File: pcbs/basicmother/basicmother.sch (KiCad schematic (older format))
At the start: 18 parts, among them IC1 ATMEGA88-P, P1 DIL16, P2 CONN_02X05, P3 CONN_02X03, P4 CONN_01X02, P5 CONN_01X02, U1 ZIGBIT_DUAL_DIP, U2 MBED, X1 18.432 MHz

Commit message: Actualizo el esquematico de la placa principal
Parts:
- P1: value DIL16 -> ZIGBIT_DIP
- P2: value CONN_02X05 -> EYES
- P3: value CONN_02X03 -> PROG_MICRO
- P4: value CONN_01X02 -> L-MOTOR
- P5: value CONN_01X02 -> R-MOTOR
- R19: renamed from R?; value R -> 1k
- gave numbers to parts that had none: 2
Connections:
- net PWM_A1 renamed PWM_L1
- net PWM_A2 renamed PWM_L2
- net PWM_B1 renamed PWM_R1
- net PWM_B2 renamed PWM_R2
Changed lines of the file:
@@
 ~SLEEP
 Text Label 8600 5050 0    60   ~ 0
-PWM_B1
+PWM_R1
 Text Label 8600 4900 0    60   ~ 0
-PWM_A2
+PWM_L2
 Text Label 8600 5450 0    60   ~ 0
 ~RESET
 Text Label 8600 4750 0    60   ~ 0
-PWM_A1
+PWM_L1
 Text Label 8600 5750 0    60   ~ 0
 ~FAULT
 Text Label 8600 5200 0    60   ~ 0
-PWM_B2
+PWM_R2
 $Comp
 L MBED U2
@@
 P 2100 1600
 F 0 "P1" H 2100 2050 60  0000 C CNN
-F 1 "DIL16" V 2100 1600 50  0000 C CNN
+F 1 "ZIGBIT_DIP" V 2100 1600 50  0000 C CNN
 F 2 "Sockets_DIP:DIP-16__300" H 2100 1600 60  0001 C CNN
 F 3 "" H 2100 1600 60  0000 C CNN
@@
 DIPSW_8
 Wire Wire Line
-	3300 5400 3500 5400
-Wire Wire Line
-	3500 5400 3750 5400
+	3300 5400 3750 5400
 Wire Wire Line
 	3750 5400 3750 4600
@@
 	3300 5050 3300 4700
 Wire Wire Line
-	1050 5400 1200 5400
-Wire Wire Line
-	1200 5400 1450 5400
+	1050 5400 1450 5400
 $Comp
 L GND #PWR02
@@
 	3300 7100 3750 7100
 Text Label 3750 6800 2    60   ~ 0
-PWM_A1
+PWM_L1
 Text Label 3750 6900 2    60   ~ 0
-PWM_A2
+PWM_L2
 Text Label 3750 7000 2    60   ~ 0
-PWM_B1
+PWM_R1
 Text Label 3750 7100 2    60   ~ 0
-PWM_B2
+PWM_R2
 Wire Wire Line
 	1450 7100 950  7100
@@
 $EndComp
 Wire Wire Line
-	7000 1950 7050 1950
-Wire Wire Line
-	7050 1950 7150 1950
+	7000 1950 7150 1950
 Wire Wire Line
 	7000 1950 7000 1900
@@
 	7750 1950 7850 1950
 Wire Wire Line
-	7850 1800 7850 1950
-Wire Wire Line
-	7850 1950 7850 2000
+	7850 1800 7850 2000
 Wire Wire Line
 	7850 1800 6700 1800
@@
 	4750 1150 4750 1200
 Wire Wire Line
-	4550 1200 4750 1200
-Wire Wire Line
-	4750 1200 4800 1200
+	4550 1200 4800 1200
 $Comp
 L +5V #PWR08
@@
 	4800 3400 4700 3400
 Wire Wire Line
-	4700 3400 4700 3500
-Wire Wire Line
-	4700 3500 4700 3600
+	4700 3400 4700 3600
 Wire Wire Line
 	4800 3500 4700 3500
@@
 P 7800 3700
 F 0 "P3" H 7800 3900 50  0000 C CNN
-F 1 "CONN_02X03" H 7800 3500 50  0000 C CNN
+F 1 "PROG_MICRO" H 7800 3500 50  0000 C CNN
 F 2 "Pin_Headers:Pin_Header_Straight_2x03" H 7800 2500 60  0001 C CNN
 F 3 "" H 7800 2500 60  0000 C CNN
@@
 P 5400 4900
 F 0 "P2" H 5400 5200 50  0000 C CNN
-F 1 "CONN_02X05" H 5400 4600 50  0000 C CNN
+F 1 "EYES" H 5400 4600 50  0000 C CNN
 F 2 "Pin_Headers:Pin_Header_Straight_2x05" H 5400 3700 60  0001 C CNN
 F 3 "" H 5400 3700 60  0000 C CNN
@@
 P 10950 5450
 F 0 "P5" H 10950 5600 50  0000 C CNN
-F 1 "CONN_01X02" V 11050 5450 50  0000 C CNN
+F 1 "R-MOTOR" H 11200 5450 50  0000 C CNN
 F 2 "Pin_Headers:Pin_Header_Straight_1x02" H 10950 5450 60  0001 C CNN
 F 3 "" H 10950 5450 60  0000 C CNN
@@
 P 10950 5150
 F 0 "P4" H 10950 5300 50  0000 C CNN
-F 1 "CONN_01X02" V 11050 5150 50  0000 C CNN
+F 1 "L-MOTOR" H 11200 5150 50  0000 C CNN
 F 2 "Pin_Headers:Pin_Header_Straight_1x02" H 10950 5150 60  0001 C CNN
 F 3 "" H 10950 5150 60  0000 C CNN
@@
 	9150 5200 8600 5200
 $Sheet
-S 10400 750  750  1000
+S 9650 950  750  1000
 U 54D57D39
 F0 "Power" 60
 F1 "power.sch" 60
-F2 "12V" I L 10400 1150 60
-F3 "14.8V" I L 10400 1350 60
-F4 "5V" I L 10400 950 60
-F5 "GND" I L 10400 1550 60
+F2 "12V" I L 9650 1350 60
+F3 "14.8V" I L 9650 1550 60
+F4 "5V" I L 9650 1150 60
+F5 "GND" I L 9650 1750 60
 $EndSheet
 Wire Wire Line
-	10400 950  10250 950
-Wire Wire Line
-	10250 950  10250 700
-Wire Wire Line
-	10400 1150 10100 1150
-Wire Wire Line
-	10100 1150 10100 700
-Wire Wire Line
-	10400 1350 9900 1350
-Wire Wire Line
-	9900 1350 9900 700
-Wire Wire Line
-	10400 1550 10050 1550
-Wire Wire Line
-	10050 1550 10050 1850
+	9650 1150 9500 1150
+Wire Wire Line
+	9500 1150 9500 900
+Wire Wire Line
+	9650 1350 9350 1350
+Wire Wire Line
+	9350 1350 9350 900
+Wire Wire Line
+	9650 1550 9150 1550
+Wire Wire Line
+	9150 1550 9150 900
+Wire Wire Line
+	9650 1750 9300 1750
+Wire Wire Line
+	9300 1750 9300 2050
 $Comp
 L GND #PWR014
 U 1 1 54D5D4C1
-P 10050 1850
-F 0 "#PWR014" H 10050 1850 30  0001 C CNN
-F 1 "GND" H 10050 1780 30  0001 C CNN
-F 2 "" H 10050 1850 60  0000 C CNN
-F 3 "" H 10050 1850 60  0000 C CNN
-	1    10050 1850
+P 9300 2050
+F 0 "#PWR014" H 9300 2050 30  0001 C CNN
+F 1 "GND" H 9300 1980 30  0001 C CNN
+F 2 "" H 9300 2050 60  0000 C CNN
+F 3 "" H 9300 2050 60  0000 C CNN
+	1    9300 2050
 	1    0    0    -1
 $EndComp
@@
 L +5V #PWR015
 U 1 1 54D5D4DC
-P 10250 700
-F 0 "#PWR015" H 10250 790 20  0001 C CNN
-F 1 "+5V" H 10250 850 30  0000 C CNN
-F 2 "" H 10250 700 60  0000 C CNN
-F 3 "" H 10250 700 60  0000 C CNN
-	1    10250 700
+P 9500 900
+F 0 "#PWR015" H 9500 990 20  0001 C CNN
+F 1 "+5V" H 9500 1050 30  0000 C CNN
+F 2 "" H 9500 900 60  0000 C CNN
+F 3 "" H 9500 900 60  0000 C CNN
+	1    9500 900
 	1    0    0    -1
 $EndComp
@@
 L +12V #PWR016
 U 1 1 54D5D5BB
-P 10100 700
-F 0 "#PWR016" H 10100 650 20  0001 C CNN
-F 1 "+12V" H 10100 850 30  0000 C CNN
-F 2 "" H 10100 700 60  0000 C CNN
-F 3 "" H 10100 700 60  0000 C CNN
-	1    10100 700
+P 9350 900
+F 0 "#PWR016" H 9350 850 20  0001 C CNN
+F 1 "+12V" H 9350 1050 30  0000 C CNN
+F 2 "" H 9350 900 60  0000 C CNN
+F 3 "" H 9350 900 60  0000 C CNN
+	1    9350 900
 	1    0    0    -1
 $EndComp
@@
 L +15V #PWR018
 U 1 1 54DE957E
-P 9900 700
-F 0 "#PWR018" H 9900 550 60  0001 C CNN
-F 1 "+15V" H 9900 840 60  0000 C CNN
-F 2 "" H 9900 700 60  0000 C CNN
-F 3 "" H 9900 700 60  0000 C CNN
-	1    9900 700
+P 9150 900
+F 0 "#PWR018" H 9150 750 60  0001 C CNN
+F 1 "+15V" H 9150 1040 60  0000 C CNN
+F 2 "" H 9150 900 60  0000 C CNN
+F 3 "" H 9150 900 60  0000 C CNN
+	1    9150 900
 	1    0    0    -1
 $EndComp
 $Sheet
-S 9500 2500 1100 950
+S 9450 2750 1100 950
 U 54DEA09E
 F0 "sound" 60
 F1 "sound.sch" 60
-F2 "In" I L 9500 3000 60
-F3 "GND" I L 9500 3250 60
-F4 "VIN" I L 9500 2600 60
-F5 "~SHD" I L 9500 2800 60
+F2 "In" I L 9450 3250 60
+F3 "GND" I L 9450 3500 60
+F4 "VIN" I L 9450 2850 60
+F5 "~SHD" I L 9450 3050 60
 $EndSheet
 $Comp
 L GND #PWR019
 U 1 1 54DEDBE5
-P 9300 3350
-F 0 "#PWR019" H 9300 3350 30  0001 C CNN
-F 1 "GND" H 9300 3280 30  0001 C CNN
-F 2 "" H 9300 3350 60  0000 C CNN
-F 3 "" H 9300 3350 60  0000 C CNN
-	1    9300 3350
-	1    0    0    -1
-$EndComp
-Wire Wire Line
-	9300 3350 9300 3250
-Wire Wire Line
-	9300 3250 9500 3250
-Wire Wire Line
-	9500 3000 9150 3000
-Text Label 9150 3000 0    60   ~ 0
+P 9250 3600
+F 0 "#PWR019" H 9250 3600 30  0001 C CNN
+F 1 "GND" H 9250 3530 30  0001 C CNN
+F 2 "" H 9250 3600 60  0000 C CNN
+F 3 "" H 9250 3600 60  0000 C CNN
+	1    9250 3600
+	1    0    0    -1
+$EndComp
+Wire Wire Line
+	9250 3600 9250 3500
+Wire Wire Line
+	9250 3500 9450 3500
+Wire Wire Line
+	9450 3250 9100 3250
+Text Label 9100 3250 0    60   ~ 0
 Audio
 Text Label 3750 7300 2    60   ~ 0
@@
 	10400 5100 10750 5100
 Wire Wire Line
-	9500 2600 9250 2600
-Wire Wire Line
-	9250 2600 9250 2400
+	9450 2850 9200 2850
+Wire Wire Line
+	9200 2850 9200 2650
 $Comp
 L +12V #PWR020
 U 1 1 5503F122
-P 9250 2400
-F 0 "#PWR020" H 9250 2350 20  0001 C CNN
-F 1 "+12V" H 9250 2550 30  0000 C CNN
-F 2 "" H 9250 2400 60  0000 C CNN
-F 3 "" H 9250 2400 60  0000 C CNN
-	1    9250 2400
-	1    0    0    -1
-$EndComp
-Wire Wire Line
-	9150 2800 9500 2800
-Text Label 9150 2800 0    60   ~ 0
+P 9200 2650
+F 0 "#PWR020" H 9200 2600 20  0001 C CNN
+F 1 "+12V" H 9200 2800 30  0000 C CNN
+F 2 "" H 9200 2650 60  0000 C CNN
+F 3 "" H 9200 2650 60  0000 C CNN
+	1    9200 2650
+	1    0    0    -1
+$EndComp
+Wire Wire Line
+	9100 3050 9450 3050
+Text Label 9100 3050 0    60   ~ 0
 ~SHD
 Text Label 950  6400 0    60   ~ 0
@@
 	10400 5750 10600 5750
 Wire Wire Line
-	10600 5750 10600 5900
-Wire Wire Line
-	10600 5900 10600 6000
+	10600 5750 10600 6000
 Wire Wire Line
 	10400 5900 10600 5900
@@
 	7300 2800 7400 2800
 Wire Wire Line
-	7400 2750 7400 2800
-Wire Wire Line
-	7400 2800 7400 2850
+	7400 2750 7400 2850
 Connection ~ 7400 2800
 Wire Wire Line
@@
 	950  6800 1450 6800
 $Comp
-L bluetooth-mod U?
+L bluetooth-mod U8
 U 1 1 5528F729
 P 5400 6700
-F 0 "U?" H 5100 7650 60  0000 C CNN
+F 0 "U8" H 5100 7650 60  0000 C CNN
 F 1 "bluetooth-mod" H 5350 5700 60  0000 C CNN
 F 2 "" H 5400 6750 60  0000 C CNN
@@
 	4400 7000 4400 6850
 $Comp
-L +3.3V #PWR?
+L +3.3V #PWR028
 U 1 1 552909F6
 P 4400 6850
-F 0 "#PWR?" H 4400 6700 50  0001 C CNN
+F 0 "#PWR028" H 4400 6700 50  0001 C CNN
 F 1 "+3.3V" H 4400 6990 50  0000 C CNN
 F 2 "" H 4400 6850 60  0000 C CNN
@@
 $EndComp
 $Comp
-L +3.3V #PWR?
+L +3.3V #PWR029
 U 1 1 55290DC4
 P 3500 5350
-F 0 "#PWR?" H 3500 5200 50  0001 C CNN
+F 0 "#PWR029" H 3500 5200 50  0001 C CNN
 F 1 "+3.3V" H 3500 5490 50  0000 C CNN
 F 2 "" H 3500 5350 60  0000 C CNN
@@
 	4400 7100 4400 7250
 $Comp
-L GND #PWR?
+L GND #PWR030
 U 1 1 5529133F
 P 4400 7250
-F 0 "#PWR?" H 4400 7250 30  0001 C CNN
+F 0 "#PWR030" H 4400 7250 30  0001 C CNN
 F 1 "GND" H 4400 7180 30  0001 C CNN
 F 2 "" H 4400 7250 60  0000 C CNN
@@
 $EndComp
 $Comp
-L GND #PWR?
+L GND #PWR031
 U 1 1 55291664
 P 6250 7150
-F 0 "#PWR?" H 6250 7150 30  0001 C CNN
+F 0 "#PWR031" H 6250 7150 30  0001 C CNN
 F 1 "GND" H 6250 7080 30  0001 C CNN
 F 2 "" H 6250 7150 60  0000 C CNN
@@
 	6250 7100 6050 7100
 $Comp
-L R R?
+L R R19
 U 1 1 552917DA
 P 6500 7100
-F 0 "R?" V 6580 7100 50  0000 C CNN
-F 1 "R" V 6500 7100 50  0000 C CNN
+F 0 "R19" V 6580 7100 50  0000 C CNN
+F 1 "1k" V 6500 7100 50  0000 C CNN
 F 2 "" V 6430 7100 30  0000 C CNN
 F 3 "" H 6500 7100 30  0000 C CNN
@@
 $EndComp
 $Comp
-L LED D?
+L LED D1
 U 1 1 5529185C
 P 6500 7500
-F 0 "D?" H 6500 7600 50  0000 C CNN
+F 0 "D1" H 6500 7600 50  0000 C CNN
 F 1 "LED" H 6500 7400 50  0000 C CNN
 F 2 "" H 6500 7500 60  0000 C CNN
@@
 	6500 7250 6500 7300
 $Comp
-L GND #PWR?
+L GND #PWR032
 U 1 1 55291BAF
 P 6500 7700
-F 0 "#PWR?" H 6500 7700 30  0001 C CNN
+F 0 "#PWR032" H 6500 7700 30  0001 C CNN
 F 1 "GND" H 6500 7630 30  0001 C CNN
 F 2 "" H 6500 7700 60  0000 C CNN

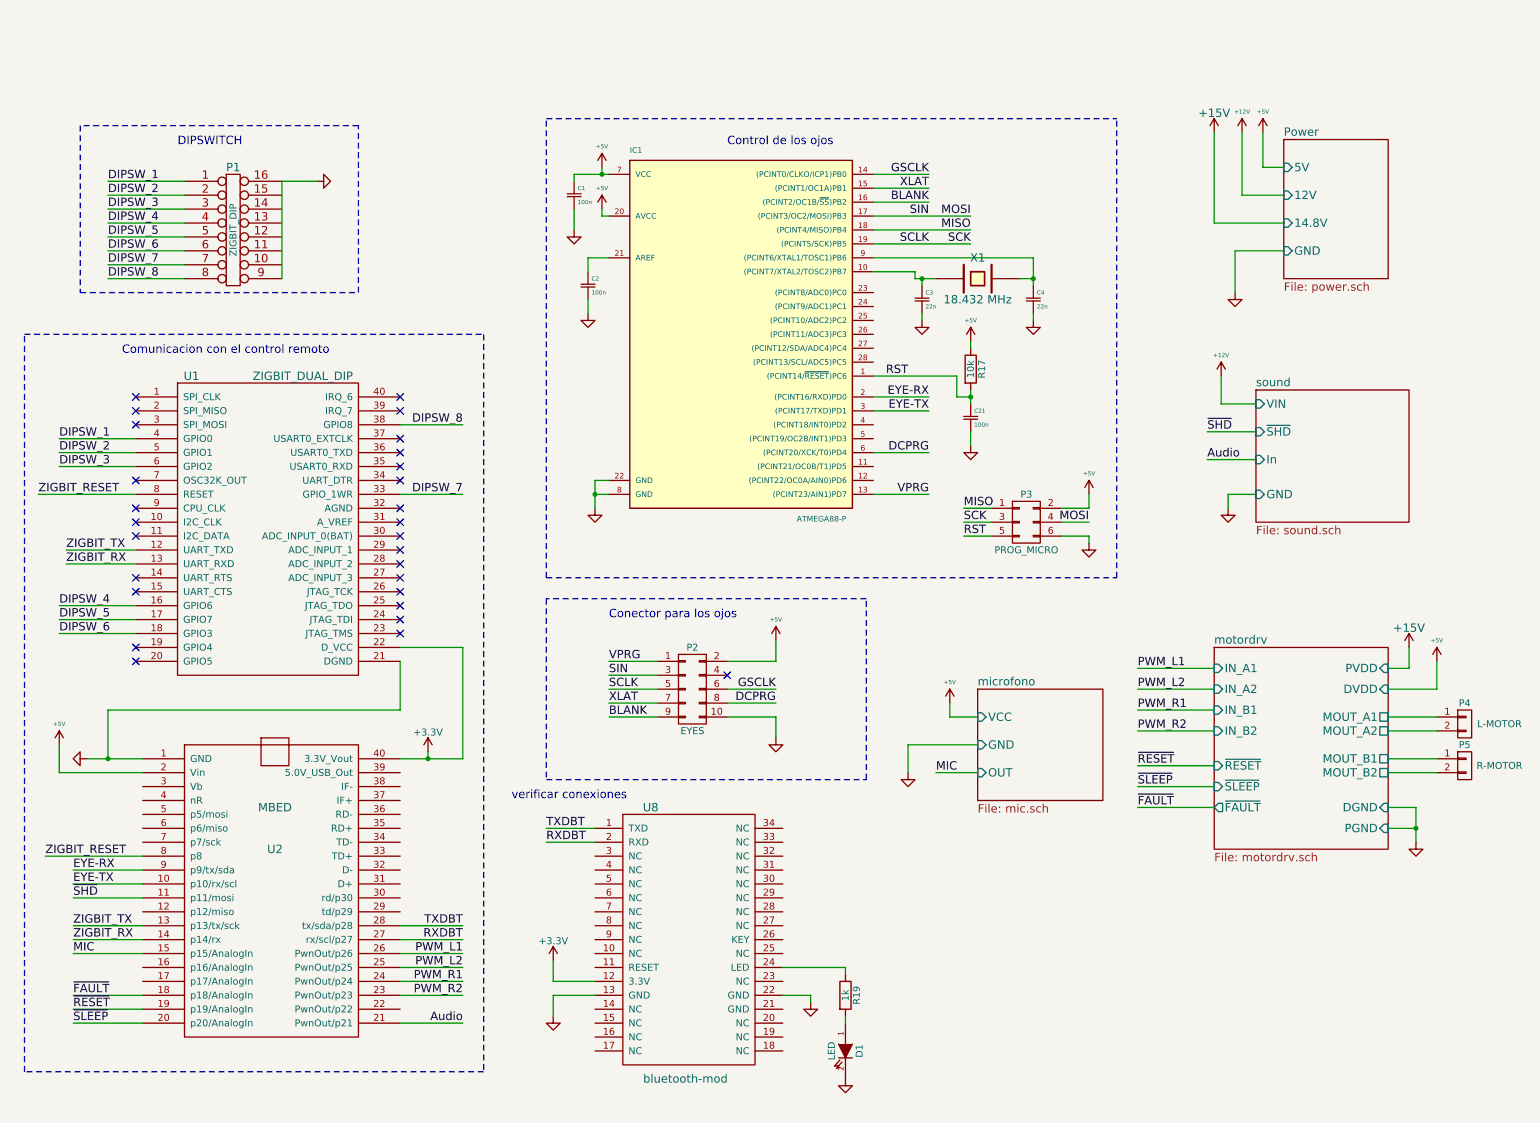
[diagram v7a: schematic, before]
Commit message: saque el micro para el control de los ojitos y lo pase a una placa aparte, ademas agregue un doble microfono
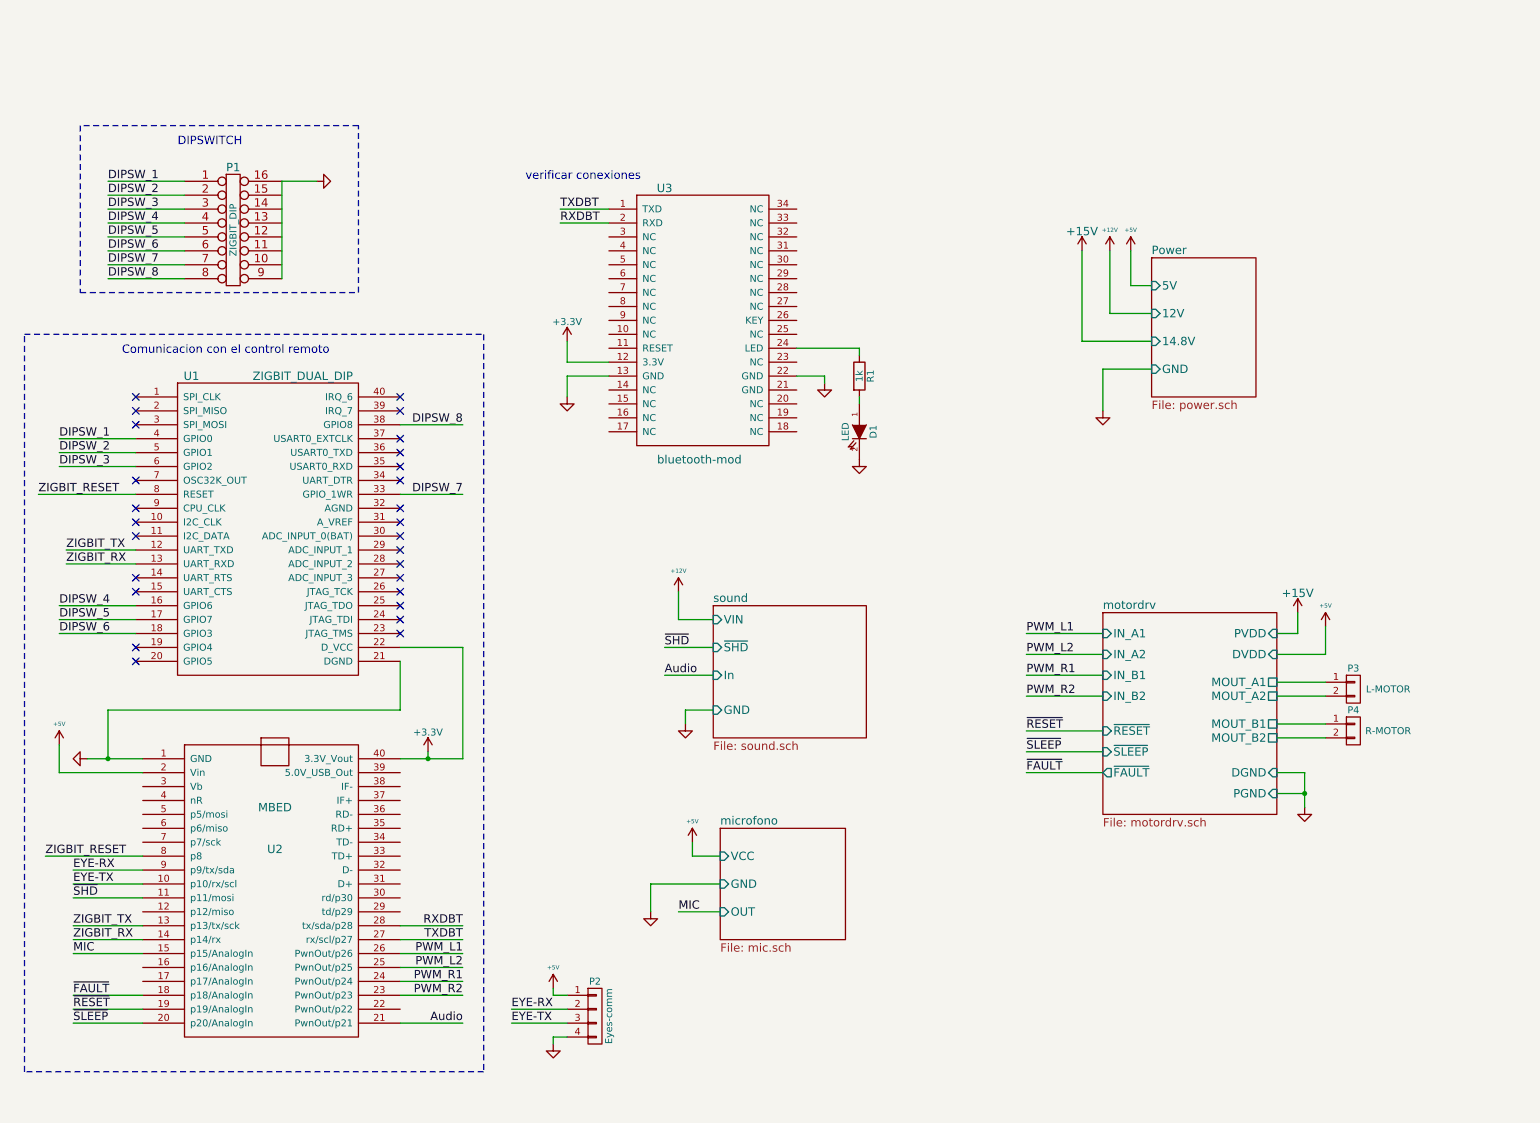
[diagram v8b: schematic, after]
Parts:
- removed C1, C2, C21: 100n, Capacitors_ThroughHole:C_Disc_D3_P2.5, symbol Csmall
- removed C3, C4: 22n, Capacitors_ThroughHole:C_Disc_D3_P2.5, symbol Csmall
- removed IC1: ATMEGA88-P, Sockets_DIP:DIP-28__300, symbol ATMEGA88-P
- removed P2: EYES, Pin_Headers:Pin_Header_Straight_2x05, symbol CONN_02X05
- removed P3: PROG_MICRO, Pin_Headers:Pin_Header_Straight_2x03, symbol CONN_02X03
- removed R17: 10k, Resistors_ThroughHole:Resistor_Horizontal_RM10mm, symbol R
- removed X1: 18.432 MHz, Crystals:Crystal_HC49-U_Vertical, symbol CRYSTAL
- added P2: Eyes-comm, Socket_Strips:Socket_Strip_Straight_1x04, symbol CONN_01X04
- D1: footprint (none) -> LEDs:LED-5MM
- P3: renamed from P4; footprint Pin_Headers:Pin_Header_Straight_1x02 -> Socket_Strips:Socket_Strip_Straight_1x02
- P4: renamed from P5; footprint Pin_Headers:Pin_Header_Straight_1x02 -> Socket_Strips:Socket_Strip_Straight_1x02
- R1: renamed from R19; footprint (none) -> Resistors_ThroughHole:Resistor_Horizontal_RM10mm
- U3: renamed from U8; footprint (none) -> Socket_Strips:Socket_Strip_Straight_2x17
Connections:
- net +5V: now also P2.1 (P1)
- net EYE-RX: now also P2.2 (P2)
- net EYE-TX: now also P2.3 (P3)
- net GND: now also P2.4 (P4)
- net RXDBT: now also U2.28 (tx/sda/p28); no longer U2.27 (rx/scl/p27)
- net TXDBT: now also U2.27 (rx/scl/p27); no longer U2.28 (tx/sda/p28)
- no-connect marks 28 -> 27
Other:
- note removed: "Conector para los ojos"
- note removed: "Control de los ojos"
- moved on the sheet: D1, P3, P4, R1, U3
